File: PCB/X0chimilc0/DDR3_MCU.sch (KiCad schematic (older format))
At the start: 1 part

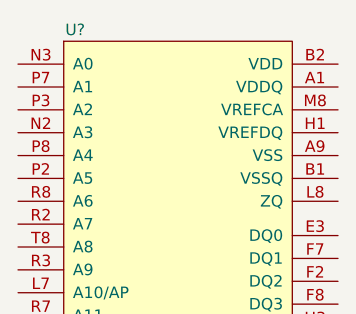
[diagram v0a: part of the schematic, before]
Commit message: Component PDFs
added relevant PDF datasheets and some minor schematic edits
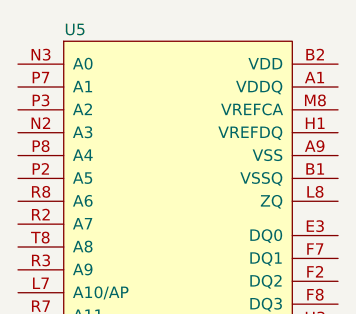
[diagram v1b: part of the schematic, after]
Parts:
- gave numbers to parts that had none: 1
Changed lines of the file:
@@
 $EndDescr
 $Comp
-L AVR-KiCAD-Lib-ICs:MT41K64M16TW-107_J-TR U?
+L AVR-KiCAD-Lib-ICs:MT41K64M16TW-107_J-TR U5
 U 1 1 5DE4E767
 P 6650 2300
-F 0 "U?" H 6700 2600 50  0000 C CNN
+F 0 "U5" H 6700 2600 50  0000 C CNN
 F 1 "MT41K64M16TW-107_J-TR" H 6850 2700 50  0001 C CNN
 F 2 "AVR-KiCAD-Lib-ICs:MT41K64M16TW_107_J_TR" H 6450 2500 50  0001 C CNN

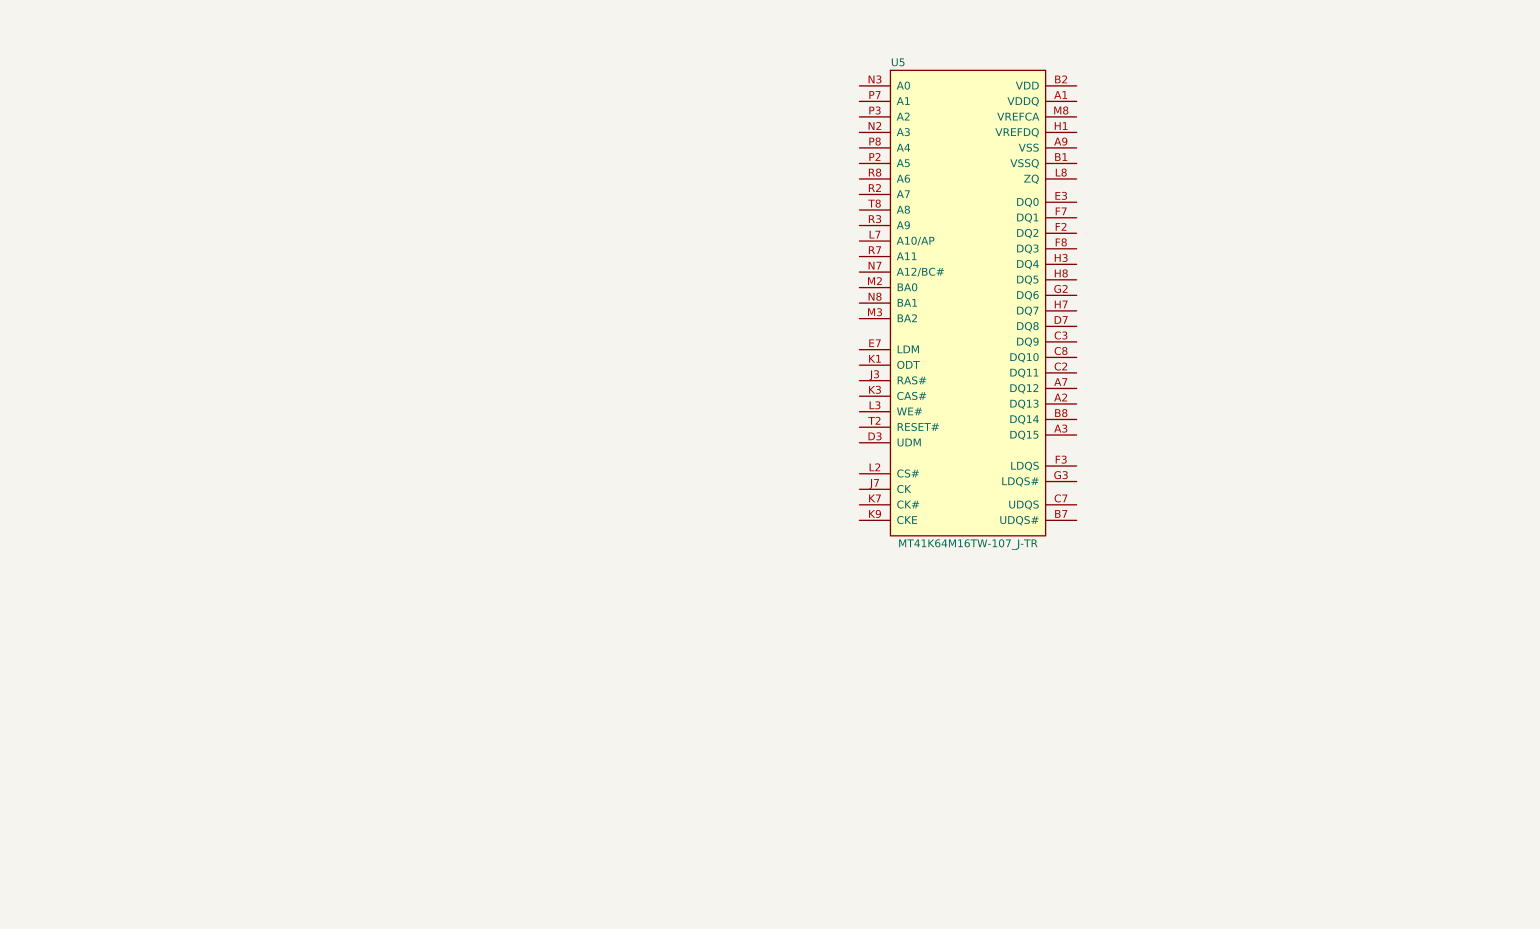
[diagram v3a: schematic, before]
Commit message: DDR3L
Memory schematic for FPGA cloned from OrangeCrab R1.0 schematic, MCU memory started. Both need finishing.
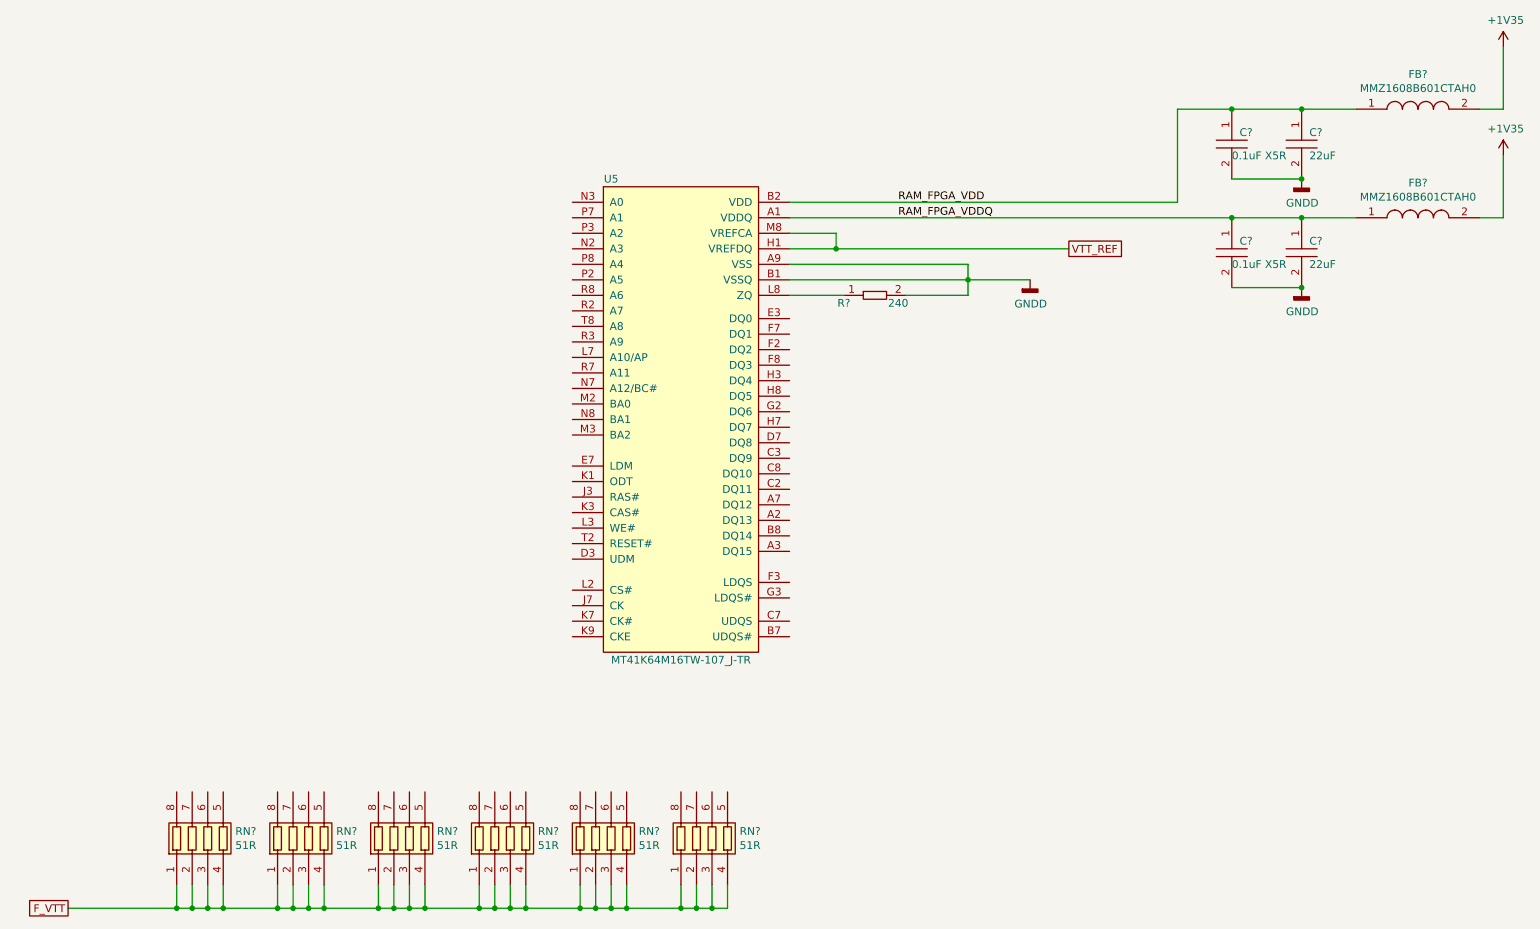
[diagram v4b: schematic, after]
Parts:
- added C? (x2): GRM188R60J226MEA0D, AVR-KiCAD-Lib-Capacitors:C0603, symbol AVR-KiCAD-Lib-Capacitors:GRM188R60J226MEA0D
- added C? (x2): C0402C104K9PACTU, AVR-KiCAD-Lib-Resistors:R0402, symbol AVR-KiCAD-Lib-Capacitors:C0402C104K9PACTU
- added FB? (x2): MMZ1608B601CTAH0, AVR-KiCAD-Lib-Resistors:R0603, symbol AVR-KiCAD-Lib-Inductors:MMZ1608B601CTAH0
- added R?: RC0402FR-07240RL, AVR-KiCAD-Lib-Resistors:R0402, symbol AVR-KiCAD-Lib-Resistors:RC0402FR-07240RL
- added RN? (x6): YC124-JR-0751RL, AVR-KiCAD-Lib-Resistors:RN0804, symbol AVR-KiCAD-Lib-Resistors:YC124-JR-0751RL
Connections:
- net RAM_FPGA_VDDQ: now reaches U5.A1 (VDDQ)
- net RAM_FPGA_VDDQ: now also C?.1, C?.1, FB?.1
- net GNDD: now reaches U5.A9 (VSS)
- net GNDD: now also U5.B1 (VSSQ), C?.2, C?.2, C?.2, C?.2, R?.2
- net RAM_FPGA_VDD: now reaches U5.B2 (VDD)
- net RAM_FPGA_VDD: now also C?.1, C?.1, FB?.1
- net VTT_REF: now reaches U5.H1 (VREFDQ)
- net VTT_REF: now also U5.M8 (VREFCA)
- net at U5.L8 (ZQ): now also R?.1
- new net +1V35: FB?.2, FB?.2
- new net F_VTT: RN?.1, RN?.1, RN?.1, RN?.1, RN?.1, RN?.1, RN?.2, RN?.2, RN?.2, RN?.2, RN?.2, RN?.2, RN?.3, RN?.3, RN?.3, RN?.3, RN?.3, RN?.3, RN?.4, RN?.4, RN?.4, RN?.4, RN?.4, RN?.4
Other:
- moved on the sheet: U5
